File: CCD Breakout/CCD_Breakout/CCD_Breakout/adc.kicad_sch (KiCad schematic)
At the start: 0 parts

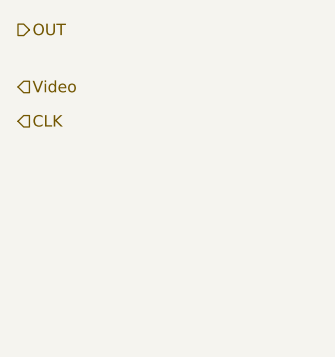
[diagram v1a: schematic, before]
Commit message: ACD Symbol Added (no functionality)
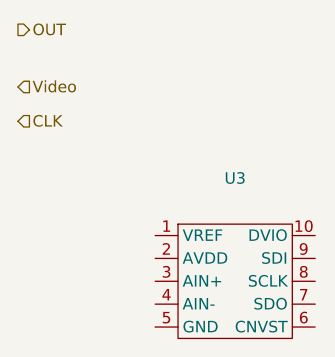
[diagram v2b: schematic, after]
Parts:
- added U3: ~, symbol 2026Training:MCP33151
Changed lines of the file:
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@@
+		)
+	)
+	(symbol
+		(lib_id "2026Training:MCP33151")
+		(at 142.24 91.44 0)
+		(unit 1)
+		(exclude_from_sim no)
+		(in_bom yes)
+		(on_board yes)
+		(dnp no)
+		(fields_autoplaced yes)
+		(property "Reference" "U3"
+			(at 142.24 80.01 0)
+			(effects
+				(font
+					(size 1.27 1.27)
+				)
+			)
+		)
+		(property "Value" "~"
+			(at 142.24 82.55 0)
+			(effects
+				(font
+					(size 1.27 1.27)
+				)
+			)
+		)
+		(property "Footprint" ""
+			(at 142.24 91.44 0)
+			(effects
+				(font
+					(size 1.27 1.27)
+				)
+				(hide yes)
+			)
+		)
+		(property "Datasheet" ""
+			(at 142.24 91.44 0)
+			(effects
+				(font
+					(size 1.27 1.27)
+				)
+				(hide yes)
+			)
+		)
+		(property "Description" ""
+			(at 142.24 91.44 0)
+			(effects
+				(font
+					(size 1.27 1.27)
+				)
+				(hide yes)
+			)
+		)
+		(pin "7"
+		)
+		(pin "3"
+		)
+		(pin "10"
+		)
+		(pin "6"
+		)
+		(pin "2"
+		)
+		(pin "4"
+		)
+		(pin "9"
+		)
+		(pin "5"
+		)
+		(pin "8"
+		)
+		(pin "1"
+		)
+		(instances
+			(project ""
+				(path "/102965ac-29c6-4f96-94a4-d07431f6d693/a53142f3-0354-4e7c-bbfe-f09d56efc2e2"
+					(reference "U3")
+					(unit 1)
+				)
+			)
 		)
 	)

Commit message: CCD Start
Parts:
- added R5, R6: R_US, symbol Device:R_US
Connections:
- net Video: now also U3.3 (AIN+)
- net +5V: now reaches U3.1 (VREF)
- net +5V: now also U3.10 (DVIO), U3.9 (SDI), R5.1
- net at U3.2 (AVDD): now also R5.2, R6.1
- net GND: now reaches U3.4 (AIN-)
- net GND: now also U3.5 (GND), R6.2

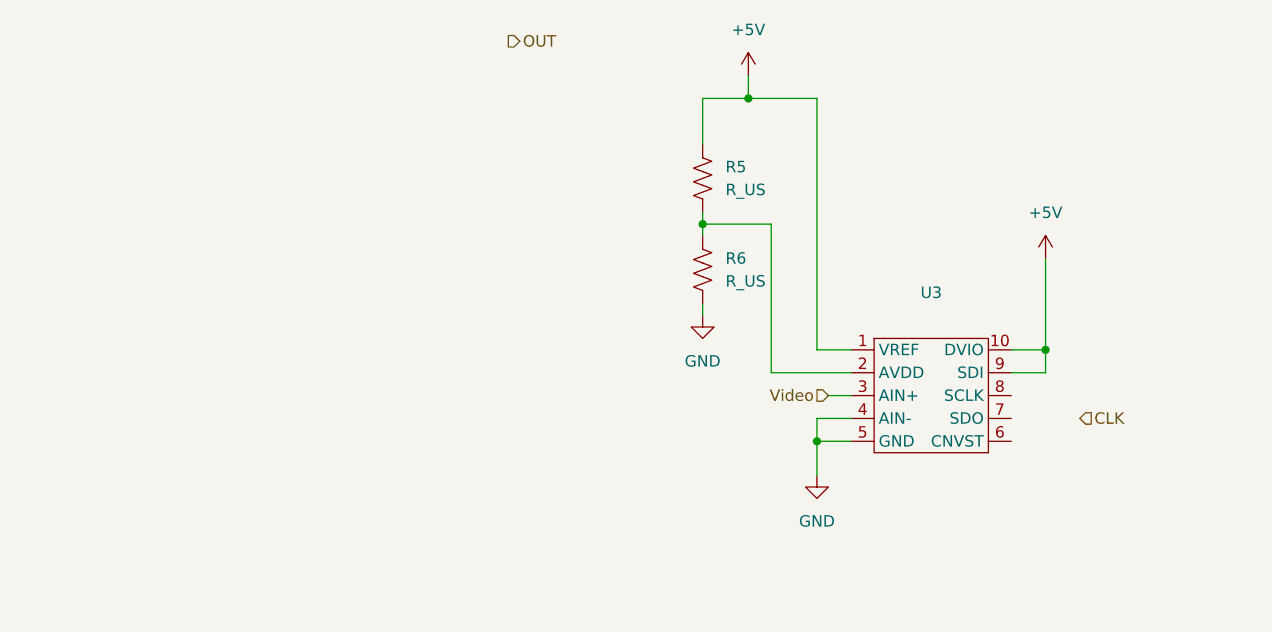
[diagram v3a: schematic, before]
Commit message: ADC Changes + Delete Fan Connector
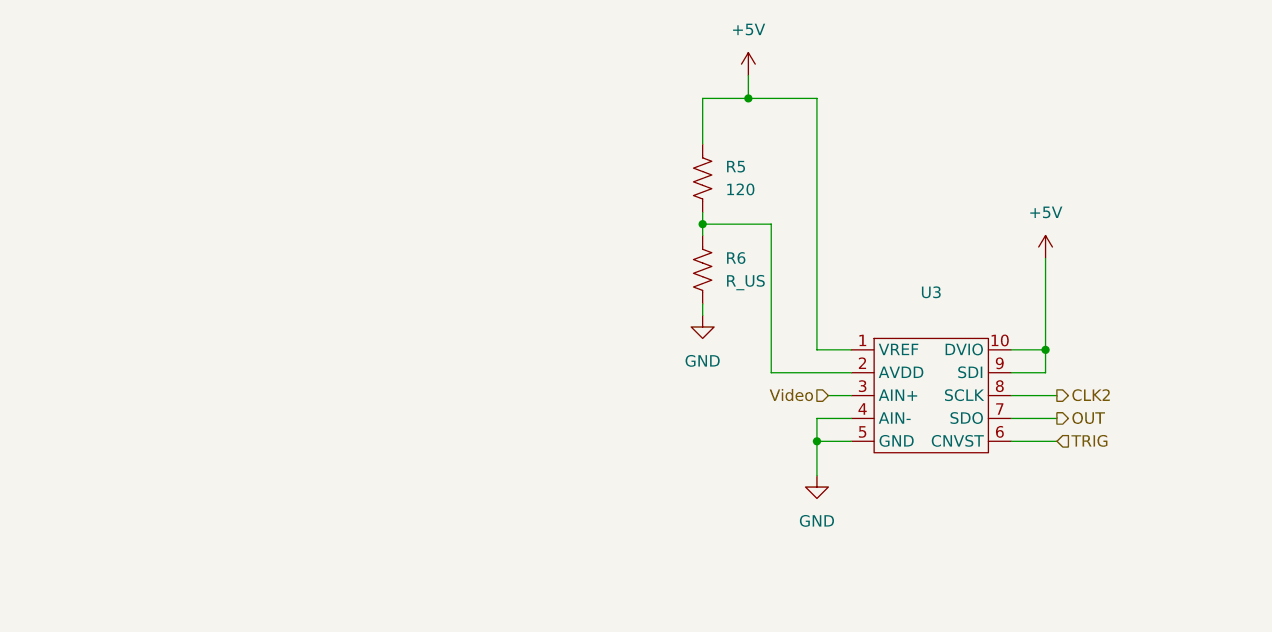
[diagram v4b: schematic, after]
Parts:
- R5: value R_US -> 120
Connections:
- net OUT: now also U3.7 (SDO)
- net TRIG: now reaches U3.6 (CNVST)
- net CLK2: now reaches U3.8 (SCLK)
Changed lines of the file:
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@@
+	(wire
+		(pts
+			(xy 151.13 96.52) (xy 156.21 96.52)
+		)
+		(stroke
+			(width 0)
+			(type default)
+		)
+	)
 	(wire
 		(pts
@@
 	(wire
 		(pts
+			(xy 151.13 91.44) (xy 156.21 91.44)
+		)
+		(stroke
+			(width 0)
+			(type default)
+		)
+	)
+	(wire
+		(pts
 			(xy 129.54 86.36) (xy 129.54 58.42)
 		)
@@
 	(wire
 		(pts
+			(xy 151.13 93.98) (xy 156.21 93.98)
+		)
+		(stroke
+			(width 0)
+			(type default)
+		)
+	)
+	(wire
+		(pts
 			(xy 124.46 72.39) (xy 116.84 72.39)
 		)
@@
 			(width 0)
 			(type default)
+		)
+	)
+	(hierarchical_label "CLK2"
+		(shape output)
+		(at 156.21 91.44 0)
+		(effects
+			(font
+				(size 1.27 1.27)
+			)
+			(justify left)
 		)
 	)
 	(hierarchical_label "OUT"
 		(shape output)
-		(at 95.25 52.07 0)
+		(at 156.21 93.98 0)
 		(effects
 			(font
@@
 		)
 	)
-	(hierarchical_label "CLK"
+	(hierarchical_label "TRIG"
 		(shape input)
-		(at 158.75 93.98 0)
+		(at 156.21 96.52 0)
 		(effects
 			(font
@@
 			)
 		)
-		(property "Value" "R_US"
+		(property "Value" "120"
 			(at 119.38 68.5799 0)
 			(effects

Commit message: Honestly a bunch of rapid changes
CCD ADC
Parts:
- added 2.2nF: C, symbol Device:C
- added R7: 100, symbol Device:R_US
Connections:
- net GND: now also 2.2nF.2
- net Video: now also R7.1; no longer U3.3 (AIN+)
- new net: 2.2nF.1, R7.2, U3.3 (AIN+)
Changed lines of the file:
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@@
+	)
+	(junction
+		(at 121.92 91.44)
+		(diameter 0)
+		(color 0 0 0 0)
 	)
 	(junction
@@
 	(wire
 		(pts
+			(xy 121.92 91.44) (xy 121.92 96.52)
+		)
+		(stroke
+			(width 0)
+			(type default)
+		)
+	)
+	(wire
+		(pts
 			(xy 154.94 86.36) (xy 151.13 86.36)
 		)
@@
 	(wire
 		(pts
+			(xy 106.68 91.44) (xy 110.49 91.44)
+		)
+		(stroke
+			(width 0)
+			(type default)
+		)
+	)
+	(wire
+		(pts
 			(xy 133.35 88.9) (xy 124.46 88.9)
 		)
@@
 	(wire
 		(pts
+			(xy 118.11 91.44) (xy 121.92 91.44)
+		)
+		(stroke
+			(width 0)
+			(type default)
+		)
+	)
+	(wire
+		(pts
+			(xy 121.92 91.44) (xy 133.35 91.44)
+		)
+		(stroke
+			(width 0)
+			(type default)
+		)
+	)
+	(wire
+		(pts
 			(xy 151.13 88.9) (xy 154.94 88.9)
 		)
@@
 	(wire
 		(pts
+			(xy 121.92 104.14) (xy 121.92 109.22)
+		)
+		(stroke
+			(width 0)
+			(type default)
+		)
+	)
+	(wire
+		(pts
 			(xy 133.35 93.98) (xy 129.54 93.98)
 		)
@@
 		(pts
 			(xy 116.84 71.12) (xy 116.84 72.39)
-		)
-		(stroke
-			(width 0)
-			(type default)
-		)
-	)
-	(wire
-		(pts
-			(xy 130.81 91.44) (xy 133.35 91.44)
 		)
 		(stroke
@@
 	(hierarchical_label "Video"
 		(shape input)
-		(at 130.81 91.44 180)
+		(at 106.68 91.44 180)
 		(effects
 			(font
@@
 	)
 	(symbol
+		(lib_id "power:GND")
+		(at 121.92 109.22 0)
+		(unit 1)
+		(exclude_from_sim no)
+		(in_bom yes)
+		(on_board yes)
+		(dnp no)
+		(fields_autoplaced yes)
+		(property "Reference" "#PWR03"
+			(at 121.92 115.57 0)
+			(effects
+				(font
+					(size 1.27 1.27)
+				)
+				(hide yes)
+			)
+		)
+		(property "Value" "GND"
+			(at 121.92 114.3 0)
+			(effects
+				(font
+					(size 1.27 1.27)
+				)
+			)
+		)
+		(property "Footprint" ""
+			(at 121.92 109.22 0)
+			(effects
+				(font
+					(size 1.27 1.27)
+				)
+				(hide yes)
+			)
+		)
+		(property "Datasheet" ""
+			(at 121.92 109.22 0)
+			(effects
+				(font
+					(size 1.27 1.27)
+				)
+				(hide yes)
+			)
+		)
+		(property "Description" "Power symbol creates a global label with name \"GND\" , ground"
+			(at 121.92 109.22 0)
+			(effects
+				(font
+					(size 1.27 1.27)
+				)
+				(hide yes)
+			)
+		)
+		(pin "1"
+		)
+		(instances
+			(project ""
+				(path "/102965ac-29c6-4f96-94a4-d07431f6d693/a53142f3-0354-4e7c-bbfe-f09d56efc2e2"
+					(reference "#PWR03")
+					(unit 1)
+				)
+			)
+		)
+	)
+	(symbol
 		(lib_id "Device:R_US")
 		(at 116.84 67.31 0)
@@
 				(path "/102965ac-29c6-4f96-94a4-d07431f6d693/a53142f3-0354-4e7c-bbfe-f09d56efc2e2"
 					(reference "R5")
+					(unit 1)
+				)
+			)
+		)
+	)
+	(symbol
+		(lib_id "Device:C")
+		(at 121.92 100.33 0)
+		(unit 1)
+		(exclude_from_sim no)
+		(in_bom yes)
+		(on_board yes)
+		(dnp no)
+		(property "Reference" "2.2nF"
+			(at 123.19 94.996 0)
+			(effects
+				(font
+					(size 1.27 1.27)
+				)
+				(justify left)
+			)
+		)
+		(property "Value" "C"
+			(at 123.19 97.536 0)
+			(effects
+				(font
+					(size 1.27 1.27)
+				)
+				(justify left)
+			)
+		)
+		(property "Footprint" ""
+			(at 122.8852 104.14 0)
+			(effects
+				(font
+					(size 1.27 1.27)
+				)
+				(hide yes)
+			)
+		)
+		(property "Datasheet" "~"
+			(at 121.92 100.33 0)
+			(effects
+				(font
+					(size 1.27 1.27)
+				)
+				(hide yes)
+			)
+		)
+		(property "Description" "Unpolarized capacitor"
+			(at 121.92 100.33 0)
+			(effects
+				(font
+					(size 1.27 1.27)
+				)
+				(hide yes)
+			)
+		)
+		(pin "1"
+		)
+		(pin "2"
+		)
+		(instances
+			(project ""
+				(path "/102965ac-29c6-4f96-94a4-d07431f6d693/a53142f3-0354-4e7c-bbfe-f09d56efc2e2"
+					(reference "2.2nF")
 					(unit 1)
 				)
@@
 					(unit 1)
 				)
+			)
+		)
+	)
+	(symbol
+		(lib_id "Device:R_US")
+		(at 114.3 91.44 90)
+		(unit 1)
+		(exclude_from_sim no)
+		(in_bom yes)
+		(on_board yes)
+		(dnp no)
+		(property "Reference" "R7"
+			(at 114.3 94.234 90)
+			(effects
+				(font
+					(size 1.27 1.27)
+				)
+			)
+		)
+		(property "Value" "100"
+			(at 114.3 96.774 90)
+			(effects
+				(font
+					(size 1.27 1.27)
+				)
+			)
+		)
+		(property "Footprint" ""
+			(at 114.554 90.424 90)
+			(effects
+				(font
+					(size 1.27 1.27)
+				)
+				(hide yes)
+			)
+		)
+		(property "Datasheet" "~"
+			(at 114.3 91.44 0)
+			(effects
+				(font
+					(size 1.27 1.27)
+				)
+				(hide yes)
+			)
+		)
+		(property "Description" "Resistor, US symbol"
+			(at 114.3 91.44 0)
+			(effects
+				(font
+					(size 1.27 1.27)
+				)
+				(hide yes)
+			)
+		)
+		(pin "1"
+		)
+		(pin "2"
+		)
+		(instances
+			(project ""
+				(path "/102965ac-29c6-4f96-94a4-d07431f6d693/a53142f3-0354-4e7c-bbfe-f09d56efc2e2"
+					(reference "R7")
+					(unit 1)
+				)

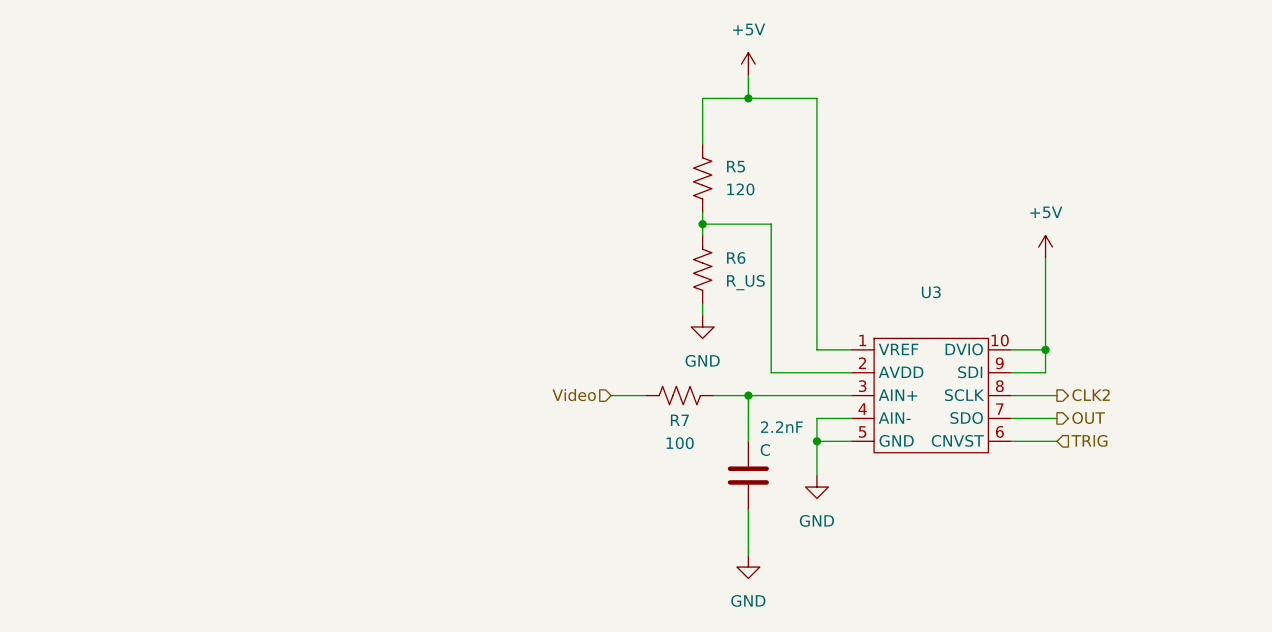
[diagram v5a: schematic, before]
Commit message: Added filtering capacitors on ADC
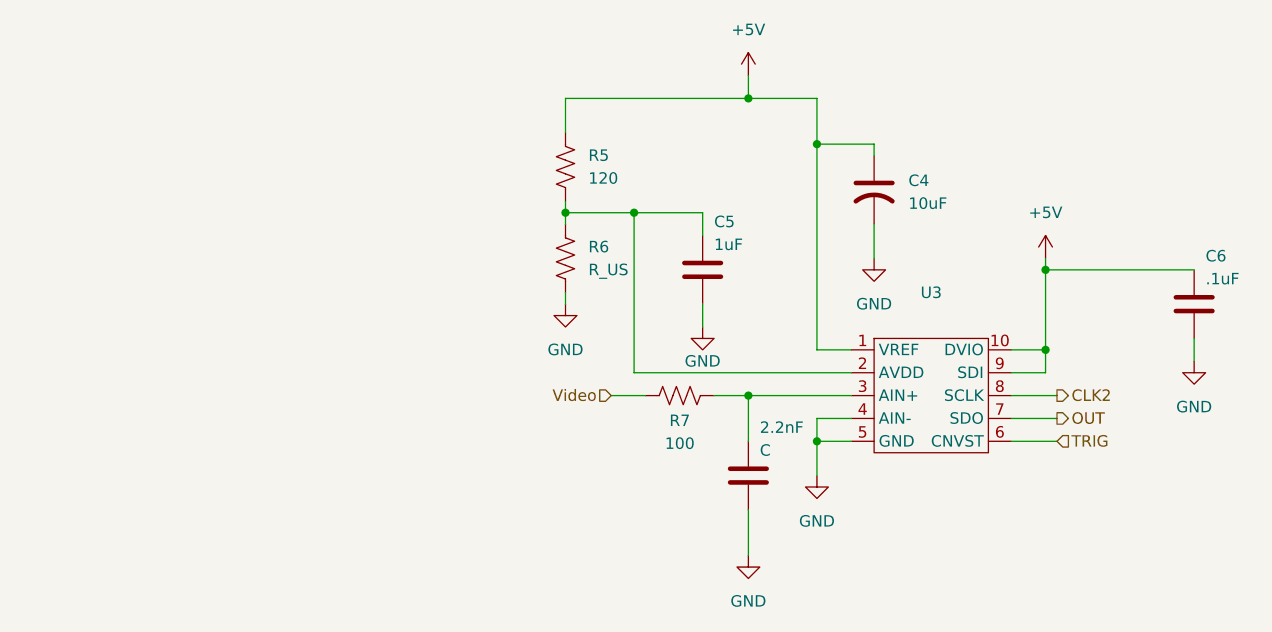
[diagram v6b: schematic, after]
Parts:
- added C4: 10uF, symbol Device:C_US
- added C5: 1uF, symbol Device:C
- added C6: .1uF, symbol Device:C
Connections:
- net +5V: now also C4.1, C6.1
- net GND: now also C4.2, C5.2, C6.2
- net at R5.2, R6.1, U3.2 (AVDD): now also C5.1
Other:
- moved on the sheet: R5, R6

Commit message: ADC 1.8 Pin
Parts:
- removed R5: 120, symbol Device:R_US
- removed R6: R_US, symbol Device:R_US
- added D1: CMDZ1L8, Diode_THT:D_DO-41_SOD81_P10.16mm_Horizontal, symbol Diode:1N47xxA
- added R2: 1000, symbol Device:R_US
- added U6: OPA1662DGK, Package_SO:VSSOP-8_3x3mm_P0.65mm, symbol Amplifier_Operational:OPA1662DGK
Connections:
- net +5V: now also R2.1
- net GND: now also D1.2 (A)
- net at C5.1, U3.2 (AVDD): now also U6.1, U6.2 (-)
- new net: D1.1 (K), R2.2, U6.3 (+)

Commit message: OpAmp IC
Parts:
- removed U6: OPA1662DGK, Package_SO:VSSOP-8_3x3mm_P0.65mm, symbol Amplifier_Operational:OPA1662DGK
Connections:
- net opIND+: now reaches D1.1 (K), R2.2
- net opIND-: now reaches C5.1, U3.2 (AVDD)
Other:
- moved on the sheet: D1, R2
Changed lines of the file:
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@@
 	)
 	(junction
-		(at 43.18 68.58)
+		(at 62.23 68.58)
 		(diameter 0)
 		(color 0 0 0 0)
@@
 	)
 	(junction
-		(at 91.44 71.12)
+		(at 97.79 71.12)
 		(diameter 0)
 		(color 0 0 0 0)
@@
 	(wire
 		(pts
+			(xy 62.23 58.42) (xy 121.92 58.42)
+		)
+		(stroke
+			(width 0)
+			(type default)
+		)
+	)
+	(wire
+		(pts
 			(xy 135.89 64.77) (xy 135.89 63.5)
 		)
@@
 	(wire
 		(pts
-			(xy 91.44 81.28) (xy 91.44 71.12)
+			(xy 97.79 81.28) (xy 97.79 71.12)
 		)
 		(stroke
@@
 	(wire
 		(pts
+			(xy 109.22 71.12) (xy 116.84 71.12)
+		)
+		(stroke
+			(width 0)
+			(type default)
+		)
+	)
+	(wire
+		(pts
 			(xy 133.35 96.52) (xy 129.54 96.52)
 		)
@@
 	(wire
 		(pts
-			(xy 43.18 68.58) (xy 74.93 68.58)
-		)
-		(stroke
-			(width 0)
-			(type default)
-		)
-	)
-	(wire
-		(pts
-			(xy 43.18 80.01) (xy 43.18 85.09)
+			(xy 62.23 80.01) (xy 62.23 85.09)
 		)
 		(stroke
@@
 	(wire
 		(pts
+			(xy 62.23 68.58) (xy 81.28 68.58)
+		)
+		(stroke
+			(width 0)
+			(type default)
+		)
+	)
+	(wire
+		(pts
 			(xy 129.54 93.98) (xy 129.54 96.52)
 		)
@@
 	(wire
 		(pts
-			(xy 43.18 68.58) (xy 43.18 72.39)
+			(xy 62.23 68.58) (xy 62.23 72.39)
 		)
 		(stroke
@@
 	(wire
 		(pts
-			(xy 116.84 71.12) (xy 109.22 71.12)
-		)
-		(stroke
-			(width 0)
-			(type default)
-		)
-	)
-	(wire
-		(pts
-			(xy 74.93 73.66) (xy 72.39 73.66)
+			(xy 81.28 73.66) (xy 78.74 73.66)
 		)
 		(stroke
@@
 	(wire
 		(pts
-			(xy 91.44 71.12) (xy 109.22 71.12)
+			(xy 97.79 71.12) (xy 109.22 71.12)
 		)
 		(stroke
@@
 	(wire
 		(pts
-			(xy 90.17 71.12) (xy 91.44 71.12)
+			(xy 96.52 71.12) (xy 97.79 71.12)
 		)
 		(stroke
@@
 	(wire
 		(pts
-			(xy 72.39 73.66) (xy 72.39 81.28)
-		)
-		(stroke
-			(width 0)
-			(type default)
-		)
-	)
-	(wire
-		(pts
-			(xy 72.39 81.28) (xy 91.44 81.28)
-		)
-		(stroke
-			(width 0)
-			(type default)
-		)
-	)
-	(wire
-		(pts
-			(xy 43.18 58.42) (xy 121.92 58.42)
-		)
-		(stroke
-			(width 0)
-			(type default)
-		)
-	)
-	(wire
-		(pts
-			(xy 43.18 66.04) (xy 43.18 68.58)
-		)
-		(stroke
-			(width 0)
-			(type default)
-		)
-	)
-	(wire
-		(pts
-			(xy 129.54 58.42) (xy 121.92 58.42)
+			(xy 78.74 73.66) (xy 78.74 81.28)
+		)
+		(stroke
+			(width 0)
+			(type default)
+		)
+	)
+	(wire
+		(pts
+			(xy 78.74 81.28) (xy 97.79 81.28)
+		)
+		(stroke
+			(width 0)
+			(type default)
+		)
+	)
+	(wire
+		(pts
+			(xy 121.92 58.42) (xy 129.54 58.42)
+		)
+		(stroke
+			(width 0)
+			(type default)
+		)
+	)
+	(wire
+		(pts
+			(xy 62.23 66.04) (xy 62.23 68.58)
 		)
 		(stroke
@@
 		)
 	)
+	(hierarchical_label "opIND-"
+		(shape output)
+		(at 81.28 73.66 0)
+		(effects
+			(font
+				(size 1.27 1.27)
+			)
+			(justify left)
+		)
+	)
 	(hierarchical_label "OUT"
 		(shape output)
 		(at 156.21 93.98 0)
+		(effects
+			(font
+				(size 1.27 1.27)
+			)
+			(justify left)
+		)
+	)
+	(hierarchical_label "opOUTD"
+		(shape input)
+		(at 96.52 71.12 180)
+		(effects
+			(font
+				(size 1.27 1.27)
+			)
+			(justify right)
+		)
+	)
+	(hierarchical_label "opIND+"
+		(shape output)
+		(at 81.28 68.58 0)
 		(effects
 			(font
@@
 	(symbol
 		(lib_id "Device:R_US")
-		(at 43.18 62.23 0)
+		(at 62.23 62.23 0)
 		(unit 1)
 		(exclude_from_sim no)
@@
 		(fields_autoplaced yes)
 		(property "Reference" "R2"
-			(at 45.72 60.9599 0)
+			(at 64.77 60.9599 0)
 			(effects
 				(font
@@
 		)
 		(property "Value" "1000"
-			(at 45.72 63.4999 0)
+			(at 64.77 63.4999 0)
 			(effects
 				(font
@@
 		)
 		(property "Footprint" ""
-			(at 44.196 62.484 90)
+			(at 63.246 62.484 90)
 			(effects
 				(font
@@
 		)
 		(property "Datasheet" "~"
-			(at 43.18 62.23 0)
+			(at 62.23 62.23 0)
 			(effects
 				(font
@@
 		)
 		(property "Description" "Resistor, US symbol"
-			(at 43.18 62.23 0)
+			(at 62.23 62.23 0)
 			(effects
 				(font
@@
 	(symbol
 		(lib_id "Diode:1N47xxA")
-		(at 43.18 76.2 270)
+		(at 62.23 76.2 270)
 		(unit 1)
 		(exclude_from_sim no)
@@
 		(fields_autoplaced yes)
 		(property "Reference" "D1"
-			(at 45.72 74.9299 90)
+			(at 64.77 74.9299 90)
 			(effects
 				(font
@@
 		)
 		(property "Value" "CMDZ1L8"
-			(at 45.72 77.4699 90)
+			(at 64.77 77.4699 90)
 			(effects
 				(font
@@
 		)
 		(property "Footprint" "Diode_THT:D_DO-41_SOD81_P10.16mm_Horizontal"
-			(at 38.735 76.2 0)
+			(at 57.785 76.2 0)
 			(effects
 				(font
@@
 		)
 		(property "Datasheet" "https://my.centralsemi.com/datasheets/CMDZ5L1-36L.PDF"
-			(at 43.18 76.2 0)
+			(at 62.23 76.2 0)
 			(effects
 				(font
@@
 		)
 		(property "Description" "DIODE ZENER 1.8V 250MW SOD323"
-			(at 43.18 76.2 0)
+			(at 62.23 76.2 0)
 			(effects
 				(font
@@
 	(symbol
 		(lib_id "power:GND")
-		(at 43.18 85.09 0)
+		(at 62.23 85.09 0)
 		(unit 1)
 		(exclude_from_sim no)
@@
 		(fields_autoplaced yes)
 		(property "Reference" "#PWR012"
-			(at 43.18 91.44 0)
+			(at 62.23 91.44 0)
 			(effects
 				(font
@@
 		)
 		(property "Value" "GND"
-			(at 43.18 90.17 0)
+			(at 62.23 90.17 0)
 			(effects
 				(font
@@
 		)
 		(property "Footprint" ""
-			(at 43.18 85.09 0)
+			(at 62.23 85.09 0)
 			(effects
 				(font
@@
 		)
 		(property "Datasheet" ""
-			(at 43.18 85.09 0)
+			(at 62.23 85.09 0)
 			(effects
 				(font
@@
 		)
 		(property "Description" "Power symbol creates a global label with name \"GND\" , ground"
-			(at 43.18 85.09 0)
+			(at 62.23 85.09 0)
 			(effects
 				(font
@@
 					(unit 1)
 				)
-			)
-		)
-	)
-	(symbol
-		(lib_id "Amplifier_Operational:OPA1662DGK")
-		(at 82.55 71.12 0)
-		(unit 1)
-		(exclude_from_sim no)
-		(in_bom yes)
-		(on_board yes)
-		(dnp no)
-		(fields_autoplaced yes)
-		(property "Reference" "U6"
-			(at 82.55 60.96 0)
-			(effects
-				(font
-					(size 1.27 1.27)
-				)
-			)
-		)
-		(property "Value" "OPA1662DGK"
-			(at 82.55 63.5 0)
-			(effects
-				(font
-					(size 1.27 1.27)
-				)
-			)
-		)
-		(property "Footprint" "Package_SO:VSSOP-8_3x3mm_P0.65mm"
-			(at 82.55 71.12 0)
-			(effects
-				(font
-					(size 1.27 1.27)
-				)
-				(hide yes)
-			)
-		)
-		(property "Datasheet" "https://www.ti.com/lit/ds/symlink/opa1662.pdf"
-			(at 82.55 71.12 0)
-			(effects
-				(font
-					(size 1.27 1.27)
-				)
-				(hide yes)
-			)
-		)
-		(property "Description" "Dual Low-Power, Low-Noise, Low-Distortion, Bipolar-Input SoundPlus Audio Operational Amplifiers, VSSOP-8"
-			(at 82.55 71.12 0)
-			(effects
-				(font
-					(size 1.27 1.27)
-				)
-				(hide yes)
-			)
-		)
-		(pin "7"
-		)
-		(pin "3"
-		)
-		(pin "5"
-		)
-		(pin "8"
-		)
-		(pin "1"
-		)
-		(pin "2"
-		)
-		(pin "6"
-		)
-		(pin "4"
-		)
-		(instances
-			(project ""
-				(path "/102965ac-29c6-4f96-94a4-d07431f6d693/a53142f3-0354-4e7c-bbfe-f09d56efc2e2"
-					(reference "U6")
-					(unit 1)
-				)
